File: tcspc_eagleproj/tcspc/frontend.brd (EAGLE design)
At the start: 45.7 x 60.6 mm, 95 parts, among them Q2 ALD1101SAL, U1 DS90LV028AQ, U3 ADCMP582, U4 LT6003_SOT23-5, U5 LT6003_SOT23-5, U6 AD53X8, X1 SMA, X2 SMA

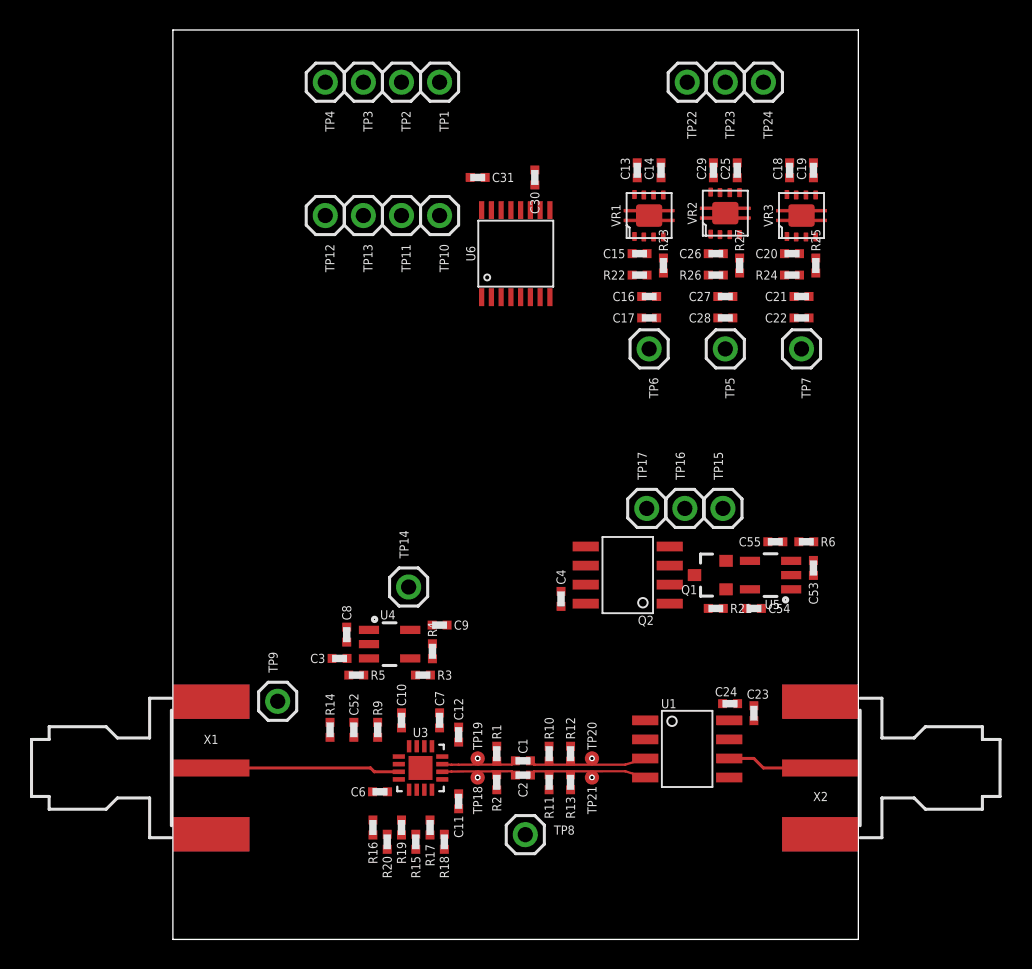
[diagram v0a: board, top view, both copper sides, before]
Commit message: Added a termination resistor to the LVDS to TTL reciever, changed a few layers on the SMA coax connector, finished up the board layout, generated gerbers to send to 3PCB.
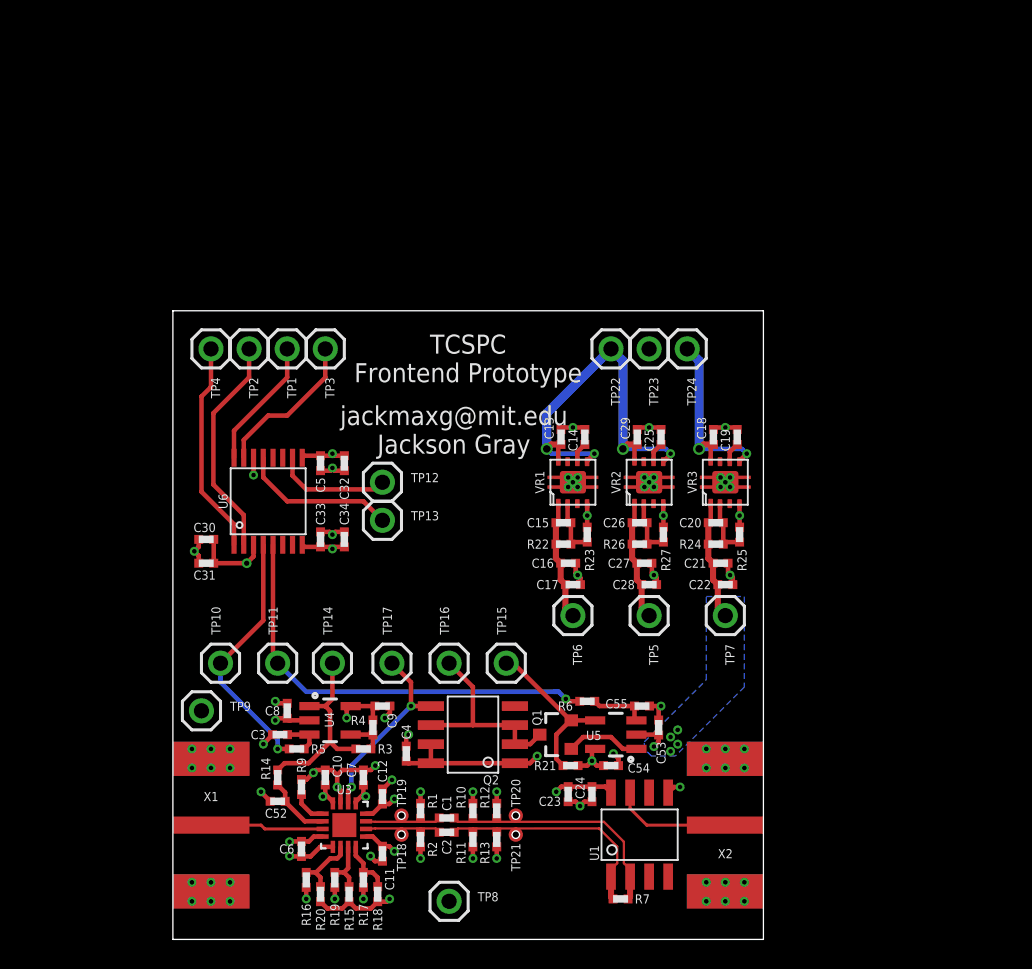
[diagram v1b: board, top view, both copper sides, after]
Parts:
- added C32, C33: 10uF, tcspc_lib:0402
- added C34, C5: 100uF, tcspc_lib:0402
- added R7: 100, tcspc_lib:0402
- moved TP10 33.2 mm to (3.17, 18.4), turned to 90 degrees
- moved C30 32.6 mm to (2.22, 26.7), turned to 180 degrees
- moved C31 31.4 mm to (2.22, 25.1)
- moved TP11 31.0 mm to (6.99, 18.4), turned to 90 degrees
- moved U6 23.3 mm to (6.35, 29.2)
- moved TP1 20.5 mm to (7.62, 39.4)
- moved TP2 20.5 mm to (5.08, 39.4)
- moved TP13 20.4 mm to (14.0, 27.9), turned to 0 degrees
- moved TP17 19.9 mm to (14.6, 18.4)
- moved TP4 19.3 mm to (2.54, 39.4)
- moved TP16 18.8 mm to (18.4, 18.4)
- moved R23 18.6 mm to (27.6, 27.0)
- moved R25 18.6 mm to (37.8, 27.0)
- moved R27 18.6 mm to (32.7, 27.0)
- moved VR2 18.6 mm to (31.8, 30.5)
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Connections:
- removed net N$14: U1.6, X2.1
- new net N$22: U1.7, X2.1
- net !CHA_LVDS_OUT: now also R7.2, U1.1; no longer U1.4
- net CHA_LVDS_OUT: now also R7.1, U1.2; no longer U1.3
- net GND: now also C32.2, C33.2, C34.2, C5.2
- net PP_P3V3_ANALOG: now also C32.1, C33.1, C34.1, C5.1
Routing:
- net GND: track 0.00 -> 70.1 mm, vias 0 -> 72
- net CHA_HYS_SET: track 0.00 -> 29.5 mm, vias 0 -> 1
- net PP_P5V_VIN: track 0.00 -> 28.1 mm, vias 0 -> 4
- net PP_P3V3_DIGITAL: track 0.00 -> 25.6 mm, vias 0 -> 9
- net PP_P3V3_ANALOG: track 0.00 -> 25.2 mm, vias 0 -> 6
- net PP_N3V3_ANALOG: track 0.00 -> 24.7 mm, vias 0 -> 8
- net CHA_THRESH_SET: track 0.00 -> 17.1 mm, vias 0 -> 1
- net T/H_DAC_!SYNC!: track 0.00 -> 14.9 mm
- net T/H_DAC_!LDAC!: track 0.00 -> 14.2 mm
- net N$2: track 0.00 -> 13.6 mm
- net PP_N5V_VIN: track 0.00 -> 13.3 mm, vias 0 -> 2
- net N$42: track 0.00 -> 12.9 mm, vias 0 -> 2
- net N$13: track 0.00 -> 12.8 mm
- net N$1: track 0.00 -> 11.1 mm
- net N$11: track 0.00 -> 10.4 mm
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- added copper zone on layer 2, net GND
- added copper zone on layer 15, net PP_N3V3_ANALOG
- added copper zone on layer 16, net PP_N3V3_ANALOG
- added copper zone on layer 15, net PP_P3V3_ANALOG
- added copper zone on layer 15, net PP_P3V3_DIGITAL
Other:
- board size 45.7 x 60.6 mm -> 39.4 x 41.9 mm
- board text added: "TCSPC Frontend Prototype"
- board text added: "jackmaxg@mit.edu Jackson Gray"

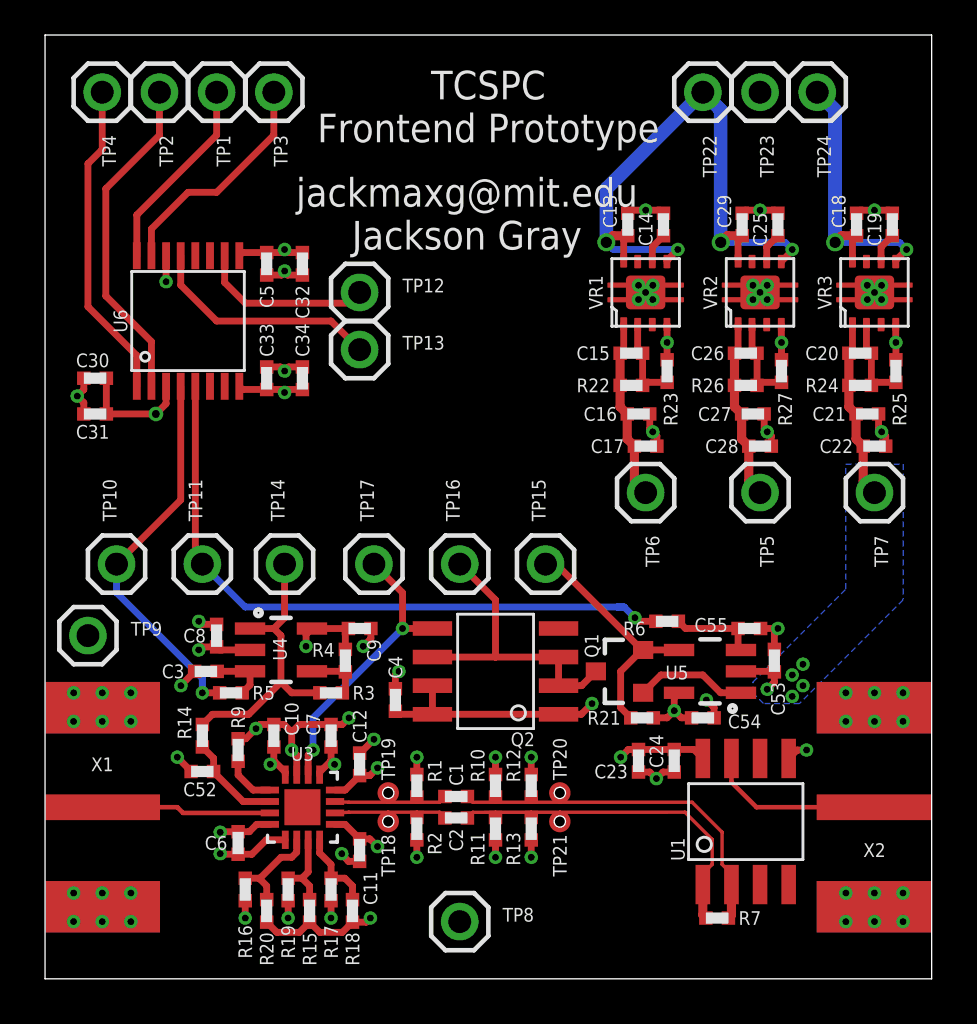
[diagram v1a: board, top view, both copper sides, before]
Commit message: Added and have been working on the THS788 carrier board for a while without committing it
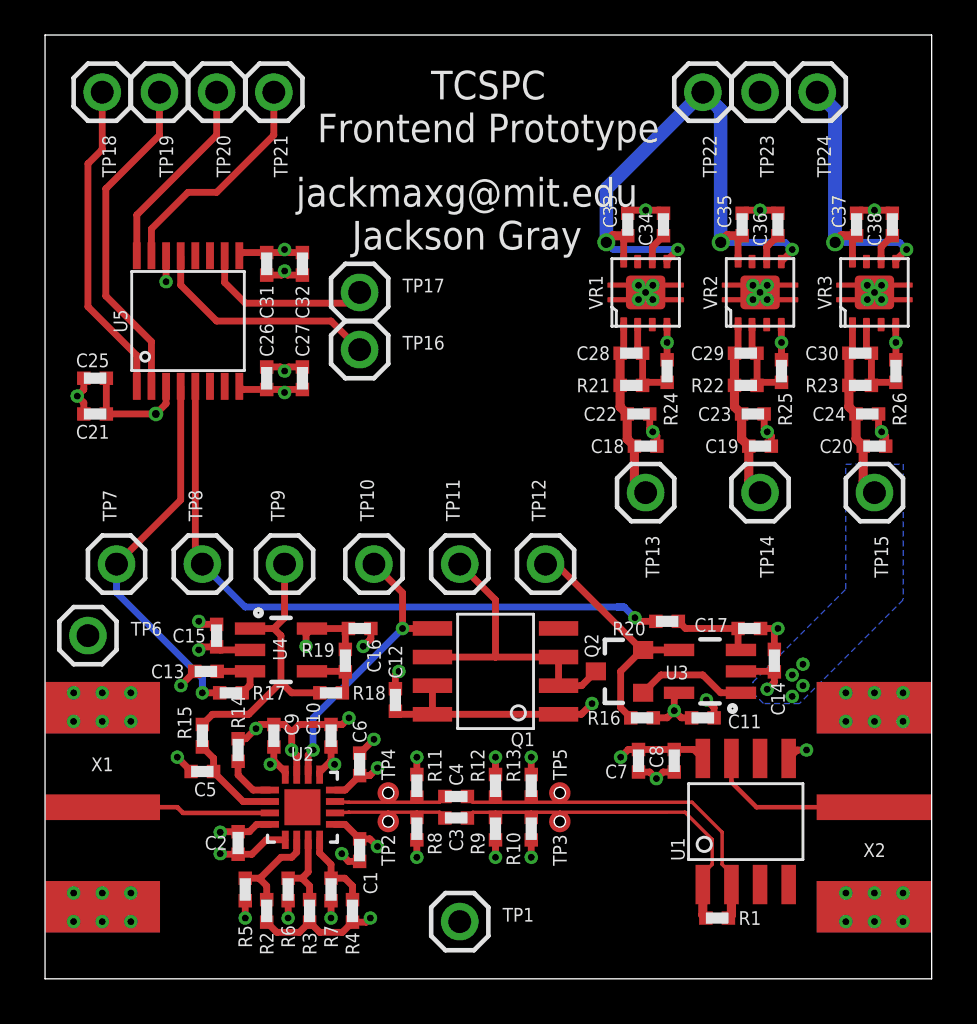
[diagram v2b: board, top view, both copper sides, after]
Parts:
- removed C52: 10nF, tcspc_lib:0402
- removed C53, C54, C55: 100nF, tcspc_lib:0402
- removed R27: 10k, tcspc_lib:0402
- removed U6: AD53X8, tcspc_lib:TSSOP-16
- added C35, C37: 100nF, tcspc_lib:0402
- added C36, C38: 10nF, tcspc_lib:0402
- added R8: 50, tcspc_lib:0402
- added U2: ADCMP582, tcspc_lib:QFN50P300X300X80-16N
- C1, C2: value 10pF -> 100nF
- C14, C15, C17, C22, C24, C25: value 10nF -> 100nF
- C18, C21, C29, C30, C8: value 100nF -> 10nF
- C3, C4: value 100nF -> 10pF
- C31, C33: value 10uF -> 100nF
- C32: value 10uF -> 10nF
- C34, C5: value 100uF -> 10nF
- Q1: value (none) -> ALD1101SAL; device tcspc_lib:SOT23-3 -> tcspc_lib:SOIC_8
- Q2: value ALD1101SAL -> (none); device tcspc_lib:SOIC_8 -> tcspc_lib:SOT23-3
- R1: value 50 -> 100
- R10: value 3.2k -> 1.8k
- R11: value 3.2k -> 50
- R12: value 1.8k -> 3.2k
- R15: value 210 -> 0
- R16: value 100 -> 5500
- R17, R18, R19, R20: value DNP -> 1k
- R2: value 50 -> DNP
- R21: value 5500 -> 17.8k
- R23: value 10k -> 17.8k
- R24, R26: value 17.8k -> 10k
- R3: value 1k -> 210
- R4, R6: value 1k -> DNP
- R5: value 1k -> 100
- R7: value 100 -> DNP
- R9: value 0 -> 3.2k
- TP1: value DAC_SCLK -> GND
- TP10: value DAC_OUT_A -> HYS_PIN
- TP11: value DAC_OUT_B -> MIRROR_GATE
- TP12: value DAC_OUT_E -> HYS_RSENSE
- TP13: value DAC_OUT_H -> P3V3A
- TP14: value THRESH -> P3V3D
- TP15: value HYS_RSENSE -> N3V3A
- TP16: value MIRROR_GATE -> DAC_OUT_H
- TP17: value HYS_PIN -> DAC_OUT_E
- TP18: value !ECL_OUT -> DAC_!LDAC!; device tcspc_lib:TESTPOINT_PAD -> tcspc_lib:1X01
- TP19: value ECL_OUT -> DAC_!SYNC!; device tcspc_lib:TESTPOINT_PAD -> tcspc_lib:1X01
- TP2: value DAC_!SYNC! -> !ECL_OUT; device tcspc_lib:1X01 -> tcspc_lib:TESTPOINT_PAD
- TP20: value LVDS_OUT -> DAC_SCLK; device tcspc_lib:TESTPOINT_PAD -> tcspc_lib:1X01
- TP21: value !LVDS_OUT -> DAC_DIN; device tcspc_lib:TESTPOINT_PAD -> tcspc_lib:1X01
- TP3: value DAC_DIN -> !LVDS_OUT; device tcspc_lib:1X01 -> tcspc_lib:TESTPOINT_PAD
- TP4: value DAC_!LDAC! -> ECL_OUT; device tcspc_lib:1X01 -> tcspc_lib:TESTPOINT_PAD
- TP5: value P3V3D -> LVDS_OUT; device tcspc_lib:1X01 -> tcspc_lib:TESTPOINT_PAD
- TP6: value P3V3A -> GND
- TP7: value N3V3A -> DAC_OUT_A
- TP8: value GND -> DAC_OUT_B
- TP9: value GND -> THRESH
- U3: value ADCMP582 -> LT6003_SOT23-5; device tcspc_lib:QFN50P300X300X80-16N -> tcspc_lib:SOT23-5
- U5: value LT6003_SOT23-5 -> AD53X8; device tcspc_lib:SOT23-5 -> tcspc_lib:TSSOP-16
- moved TP1 38.4 mm to (18.4, 2.54), turned to 0 degrees
- moved TP18 34.8 mm to (2.54, 39.4)
- moved TP21 34.8 mm to (10.2, 39.4)
- moved TP3 34.8 mm to (22.9, 6.99)
- moved TP20 34.6 mm to (7.62, 39.4), turned to 270 degrees
- moved C21 34.3 mm to (2.22, 25.1), turned to 180 degrees
- moved C30 34.0 mm to (36.2, 27.8), turned to 0 degrees
- moved TP2 33.9 mm to (15.2, 6.99)
- moved TP7 33.8 mm to (3.17, 18.4), turned to 90 degrees
- moved TP4 33.6 mm to (15.2, 8.26), turned to 90 degrees
- moved TP19 32.7 mm to (5.08, 39.4), turned to 270 degrees
- moved C25 31.1 mm to (2.22, 26.7), turned to 180 degrees
- moved U5 27.9 mm to (6.35, 29.2)
- moved C13 27.3 mm to (7.14, 13.7), turned to 180 degrees
- moved TP6 25.6 mm to (1.91, 15.2), turned to 0 degrees
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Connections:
- net !CHA_LVDS_OUT: now also C3.2, R1.2, R10.1, R9.2, TP3.TP; no longer C2.2, R11.2, R13.1, R7.2, TP21.TP
- net CHA_HYS_SET: now also R20.1, TP8.1, U5.5; no longer R6.1, TP11.1, U6.5
- net CHA_LVDS_OUT: now also C4.2, R1.1, R12.2, R13.1, TP5.TP; no longer C1.2, R10.2, R12.1, R7.1, TP20.TP
- net CHA_THRESH_SET: now also R17.1, TP7.1, U5.4; no longer R5.1, TP10.1, U6.4
- net GND: now also C1.2, C10.1, C15.2, C2.2, C20.2, C26.2, C35.2, C36.2, C37.2, C38.2, C5.1, C7.2, R10.2, R11.2, R14.1, R24.1, R26.1, R3.2, R4.2, R8.2, TP1.1, TP6.1, U2.15, U2.4, U5.14; no longer C10.2, C28.2, C29.2, C3.2, C30.2, C4.2, C5.2, C52.1, C53.2, C54.2, C55.2, C7.1, R1.2, R12.2, R15.2, R18.2, R20.2, R23.1, R27.1, R9.1, TP8.1, TP9.1, U3.15, U3.4, U6.14
- net N$1: now also Q2.2, R16.2, TP12.1, U3.4; no longer Q1.2, R21.2, TP15.1, U5.4
- net N$10: now also Q2.1, U3.1; no longer Q1.1, U5.1
- net N$11: now also TP16.1, U5.13; no longer TP13.1, U6.13
- net N$12: now also R18.1, R19.2; no longer R3.1, R4.2
- net N$13: now also R15.1, R18.2, TP9.1; no longer R14.1, R3.2, TP14.1
- net N$16: now also C36.1; no longer C25.1
- net N$17: now also C17.1, R20.2, U3.3; no longer C55.1, R6.2, U5.3
- net N$18: now also U2.3; no longer U3.3
- net N$19: now also C34.1; no longer C14.1
- net N$2: now also Q1.2, Q1.6, TP11.1; no longer Q2.2, Q2.6, TP16.1
- net N$21: now also C29.2, R22.2, R25.2; no longer C26.2, R26.2, R27.2
- net N$25: now also C38.1; no longer C19.1
- net N$3: now also C3.1, R8.1, TP2.TP, U2.10; no longer C2.1, R2.1, TP18.TP, U3.10
- net N$37: now also C5.2, R15.2, U2.2; no longer C52.2, R14.2, U3.2
- net N$38: now also R4.1, R7.2, U2.8; no longer R17.2, R18.1, U3.8
- net N$39: now also R3.1, R6.2, U2.7; no longer R15.1, R19.2, U3.7
- net N$4: now also C30.2, R23.2, R26.2; no longer C20.2, R24.2, R25.2
- net N$41: now also R2.1, R5.2, U2.6; no longer R16.2, R20.1, U3.6
- net N$42: now also Q1.5, TP10.1, U2.14; no longer Q2.5, TP17.1, U3.14
- net N$5: now also C28.2, R21.2, R24.2; no longer C15.2, R22.2, R23.2
- net N$6: now also C4.1, R11.1, TP4.TP, U2.11; no longer C1.1, R1.1, TP19.TP, U3.11
- net N$7: now also R14.2, U2.1; no longer R9.2, U3.1
- net N$8: now also TP17.1, U5.10; no longer TP12.1, U6.10
- net N$9: now also C13.1, R17.2; no longer C3.1, R5.2
- net PP_N3V3_ANALOG: now also C10.2, C12.1, C14.1, C15.1, C24.1, C30.1, Q1.1, Q1.7, Q1.8, R23.1, TP15.1, U2.13, U3.2; no longer C21.1, C22.1, C4.1, C53.1, C7.2, C8.1, Q2.1, Q2.7, Q2.8, R24.1, TP7.1, U3.13, U5.2
- net PP_N5V_VIN: now also C37.1; no longer C18.1
- net PP_P3V3_ANALOG: now also C11.1, C18.1, C2.1, C22.1, C26.1, C27.1, C28.1, C31.1, R16.1, R19.1, TP13.1, U2.16, U2.5, U5.8, U5.9; no longer C10.1, C15.1, C17.1, C33.1, C34.1, C5.1, C54.1, C6.1, R22.1, R4.1, TP6.1, U3.16, U5.5, U6.8, U6.9
- net PP_P3V3_DIGITAL: now also C1.1, C19.1, C21.1, C25.1, C29.1, C6.1, C7.1, C8.1, R12.1, R22.1, R5.1, R6.1, R7.1, R9.1, TP14.1, U2.12, U2.9, U5.3; no longer C11.1, C12.1, C24.1, C26.1, C27.1, C28.1, C30.1, C31.1, R10.1, R11.1, R16.1, R17.1, R19.1, R26.1, TP5.1, U3.12, U3.9, U6.3
- net PP_P5V_VIN: now also C33.1, C35.1; no longer C13.1, C29.1
- net T/H_DAC_!LDAC!: now also TP18.1, U5.1; no longer TP4.1, U6.1
- net T/H_DAC_!SYNC!: now also TP19.1, U5.2; no longer TP2.1, U6.2
- net T/H_DAC_DIN: now also TP21.1, U5.15; no longer TP3.1, U6.15
- net T/H_DAC_SCLK: now also TP20.1, U5.16; no longer TP1.1, U6.16
